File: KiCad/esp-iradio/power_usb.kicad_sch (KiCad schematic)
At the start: 58 parts, among them J201 USB-C TYPE-C-31-M-12, J202 Li-Po cell (JST-PH), Q201 MMBT3904, Q202 MMBT3904, Q203 DMG2305UX-7, SW201 RESET, SW202 BOOT, SW203 ON/OFF MSK12C02, U201 BQ24074RGTR, U202 USBLC6-2SC6, U203 CH340C, U204 DW01A, U205 FS8205A, U206 AP7361C-33Y5-13, U207 TPLP5907MFX-3.3

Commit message: KiCad Rev B: review changes agreed with Grok
Co-Authored-By: Claude Opus 5.5 <noreply@anthropic.com>
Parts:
- added C214: 100nF, Capacitor_SMD:C_0603_1608Metric, symbol Elektuur:C
- added TP203: ESP_EN, TestPoint:TestPoint_Pad_D1.5mm, symbol Connector:TestPoint
- added TP204: ESP_IO0, TestPoint:TestPoint_Pad_D1.5mm, symbol Connector:TestPoint
- added TP205: TXD0, TestPoint:TestPoint_Pad_D1.5mm, symbol Connector:TestPoint
- added TP206: RXD0, TestPoint:TestPoint_Pad_D1.5mm, symbol Connector:TestPoint
- added TP207: GND, TestPoint:TestPoint_Pad_D1.5mm, symbol Connector:TestPoint
- F201: value 1.5A hold -> 2A hold 16V; LCSC C22379952 -> C22374899
- R203: value 33k -> 330k
- R204: value 22k -> 220k
- R210: value 1.1k -> 1.13k
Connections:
- net ESP_EN: now also TP203.1
- net ESP_IO0: now also TP204.1
- net GND: now also C214.2 (-), TP207.1
- net RXD0: now also TP206.1
- net TXD0: now also TP205.1
- net VBUS: no longer D201.1 (K-)
- net VBUS_SENSE: now also C214.1 (+)
- net at C201.1 (+), F201.2 (-), R203.1 (+)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: now also D201.1 (K-)
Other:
- note added: "CHARGER: BQ24074 power path (OUT = VSYS), 0.8 A charge, 1.37 A input"
- note added: "ILIM 1.13k: input 1.37 A, ISET 1.1k: charge 0.8 A"
- note added: "RECOVERY PADS: flash the ESP32 without USB-C / CH340C (switch on, +3V3 = TP4)"
- note removed: "CHARGER: BQ24074 power path (OUT = VSYS), 0.8 A charge, 1.4 A input"
- note removed: "ILIM 1.1k: input 1.4 A, ISET 1.1k: charge 0.8 A"

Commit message: KiCad Rev B: USBLC6 VBUS behind the fuse (third review round)
Co-Authored-By: Claude Opus 5.5 <noreply@anthropic.com>
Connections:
- net VBUS: no longer U202.5 (VBUS)
- net VIN: now reaches C201.1 (+), D201.1 (K-), F201.2 (-), R203.1 (+), TP201.1, U201.13 (IN)
- net VIN: now also U202.5 (VBUS)
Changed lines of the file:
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@@
 		)
 	)
-	(label "VBUS"
+	(label "VIN"
 		(at 60.96 91.44 90)
 		(effects
@@
 		)
 	)
+	(label "VIN"
+		(at 116.84 40.64 0)
+		(effects
+			(font
+				(size 1.27 1.27)
+			)
+			(justify left bottom)
+		)
+	)
 	(no_connect
 		(at 162.56 53.34)
@@
 	(wire
 		(pts
-			(xy 101.6 40.64) (xy 152.4 40.64)
-		)
-		(stroke
+			(xy 101.6 40.64) (xy 116.84 40.64)
+		)
+		(stroke
+			(width 0)
+			(type default)
+		)
+	)
+	(wire
+		(pts
+			(xy 116.84 40.64) (xy 152.4 40.64)
+		)
+		(stroke

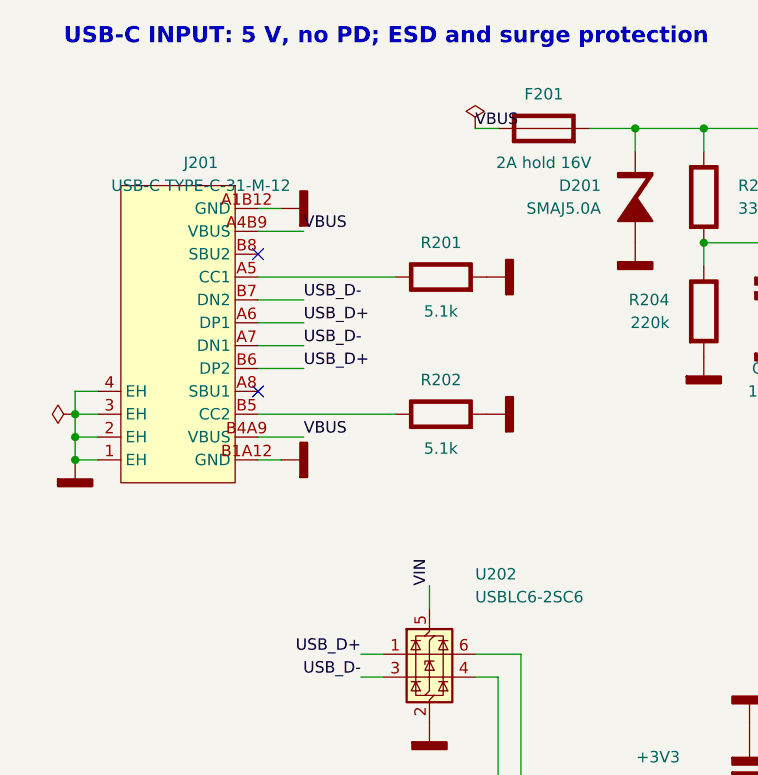
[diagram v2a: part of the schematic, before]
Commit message: KiCad Rev B: first layout (80 x 60 mm, 4 layers, autorouted)
Co-Authored-By: Claude Opus 5.5 <noreply@anthropic.com>
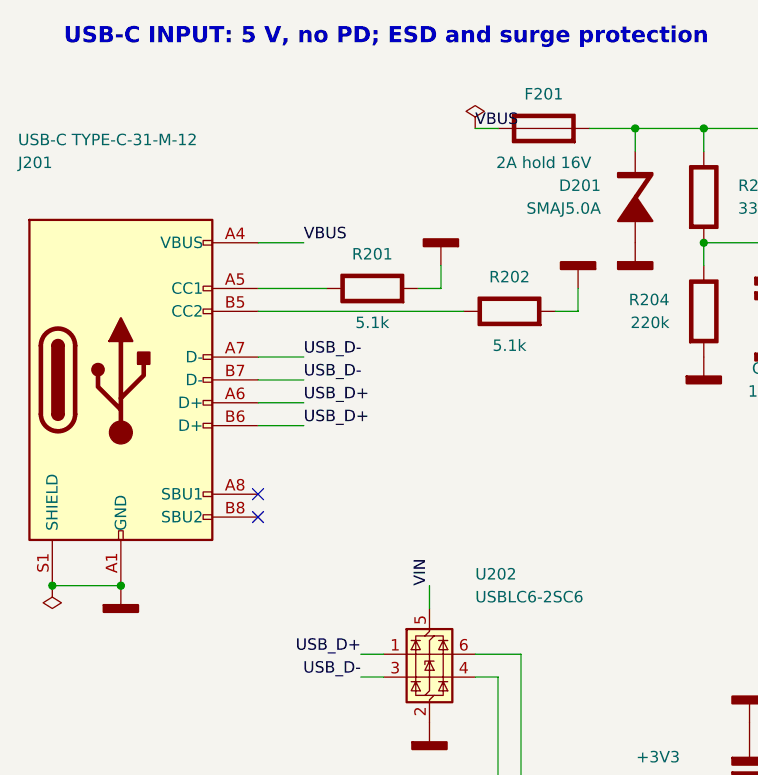
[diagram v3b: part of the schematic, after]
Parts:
- removed J201: USB-C TYPE-C-31-M-12, lcsc:USB-C_SMD-TYPE-C-31-M-12_1, symbol lcsc:TYPE-C-31-M-12
- added J201: USB-C TYPE-C-31-M-12, Connector_USB:USB_C_Receptacle_HRO_TYPE-C-31-M-12, symbol Connector:USB_C_Receptacle_USB2.0_16P
- TP201, TP202, TP203, TP204, TP205, TP206, TP207: now left out of the parts list
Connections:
- net GND: now also J201.A1 (GND), J201.A12 (GND), J201.B1 (GND), J201.B12 (GND), J201.S1 (SHIELD)
- net USB_D+: now also J201.A6 (D+), J201.B6 (D+)
- net USB_D-: now also J201.A7 (D-), J201.B7 (D-)
- net VBUS: now also J201.A4 (VBUS), J201.A9 (VBUS), J201.B4 (VBUS), J201.B9 (VBUS)
- net at R202.1 (+): now also J201.B5 (CC2)
- net at R201.1 (+): now also J201.A5 (CC1)

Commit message: BQ24074RGTT (C2861252) for U201, one BOM line per LCSC part
Co-Authored-By: Claude Opus 5.5 <noreply@anthropic.com>
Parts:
- U201: value BQ24074RGTR -> BQ24074RGTT; LCSC C54313 -> C2861252
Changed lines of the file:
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@@
 			)
 		)
-		(property "Value" "BQ24074RGTR"
+		(property "Value" "BQ24074RGTT"
 			(at 172.72 46.99 0)
 			(effects
@@
 			)
 		)
-		(property "LCSC" "C54313"
+		(property "LCSC" "C2861252"
 			(at 175.26 63.5 0)
 			(effects

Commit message: KiCad Rev C: hand assembly (1206), RCA outputs, display/encoder/connectors floor plan
Co-Authored-By: Claude Opus 5.5 <noreply@anthropic.com>
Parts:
- C201, C202, C203, C208, C209, C210: footprint Capacitor_SMD:C_0805_2012Metric -> Capacitor_SMD:C_1206_3216Metric
- C204, C205, C206, C207, C211, C212, C213, C214: footprint Capacitor_SMD:C_0603_1608Metric -> Capacitor_SMD:C_1206_3216Metric
- D202: footprint LED_SMD:LED_0603_1608Metric -> LED_SMD:LED_1206_3216Metric; LCSC C2286 -> C965822
- D203: footprint LED_SMD:LED_0603_1608Metric -> LED_SMD:LED_1206_3216Metric; LCSC C12624 -> C965825
- D204, D205: value BAT54WS -> BAT54W; footprint Diode_SMD:D_SOD-323 -> Diode_SMD:D_SOD-123; LCSC C7502694 -> C7502705
- R201, R202, R203, R204, R205, R206, R207, R208, R209, R210, R211, R212, R213, R214, R215, R216, R217, R218, R219, R220, R221: footprint Resistor_SMD:R_0603_1608Metric -> Resistor_SMD:R_1206_3216Metric
- RT201: footprint Resistor_SMD:R_0603_1608Metric -> Resistor_SMD:R_0805_2012Metric; LCSC C13564 -> C2889056
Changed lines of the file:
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@@
 			)
 		)
-		(property "Footprint" "Resistor_SMD:R_0603_1608Metric"
+		(property "Footprint" "Resistor_SMD:R_1206_3216Metric"
 			(at 54.61 58.42 0)
 			(effects
@@
 			)
 		)
-		(property "Footprint" "Resistor_SMD:R_0603_1608Metric"
+		(property "Footprint" "Resistor_SMD:R_1206_3216Metric"
 			(at 69.85 60.96 0)
 			(effects
@@
 			)
 		)
-		(property "Footprint" "Resistor_SMD:R_0603_1608Metric"
+		(property "Footprint" "Resistor_SMD:R_1206_3216Metric"
 			(at 91.44 48.26 0)
 			(effects
@@
 			)
 		)
-		(property "Footprint" "Resistor_SMD:R_0603_1608Metric"
+		(property "Footprint" "Resistor_SMD:R_1206_3216Metric"
 			(at 91.44 60.96 0)
 			(effects
@@
 			)
 		)
-		(property "Footprint" "Capacitor_SMD:C_0603_1608Metric"
+		(property "Footprint" "Capacitor_SMD:C_1206_3216Metric"
 			(at 99.06 58.42 0)
 			(effects
@@
 			)
 		)
-		(property "Footprint" "Capacitor_SMD:C_0603_1608Metric"
+		(property "Footprint" "Capacitor_SMD:C_1206_3216Metric"
 			(at 96.52 111.76 0)
 			(effects
@@
 			)
 		)
-		(property "Footprint" "Resistor_SMD:R_0603_1608Metric"
+		(property "Footprint" "Resistor_SMD:R_1206_3216Metric"
 			(at 114.3 137.16 0)
 			(effects
@@
 			)
 		)
-		(property "Footprint" "Resistor_SMD:R_0603_1608Metric"
+		(property "Footprint" "Resistor_SMD:R_1206_3216Metric"
 			(at 114.3 162.56 0)
 			(effects
@@
 			)
 		)
-		(property "Footprint" "Resistor_SMD:R_0603_1608Metric"
+		(property "Footprint" "Resistor_SMD:R_1206_3216Metric"
 			(at 139.7 121.92 0)
 			(effects
@@
 			)
 		)
-		(property "Footprint" "Capacitor_SMD:C_0603_1608Metric"
+		(property "Footprint" "Capacitor_SMD:C_1206_3216Metric"
 			(at 147.32 132.08 0)
 			(effects
@@
 			)
 		)
-		(property "Footprint" "Resistor_SMD:R_0603_1608Metric"
+		(property "Footprint" "Resistor_SMD:R_1206_3216Metric"
 			(at 139.7 147.32 0)
 			(effects
@@
 			)
 		)
-		(property "Footprint" "Capacitor_SMD:C_0805_2012Metric"
+		(property "Footprint" "Capacitor_SMD:C_1206_3216Metric"
 			(at 152.4 45.72 0)
 			(effects
@@
 			)
 		)
-		(property "Footprint" "Resistor_SMD:R_0603_1608Metric"
+		(property "Footprint" "Resistor_SMD:R_1206_3216Metric"
 			(at 116.84 93.98 0)
 			(effects
@@
 			)
 		)
-		(property "Footprint" "Resistor_SMD:R_0603_1608Metric"
+		(property "Footprint" "Resistor_SMD:R_1206_3216Metric"
 			(at 147.32 93.98 0)
 			(effects
@@
 			)
 		)
-		(property "Footprint" "Resistor_SMD:R_0603_1608Metric"
+		(property "Footprint" "Resistor_SMD:R_1206_3216Metric"
 			(at 160.02 93.98 0)
 			(effects
@@
 			)
 		)
-		(property "Footprint" "Capacitor_SMD:C_0805_2012Metric"
+		(property "Footprint" "Capacitor_SMD:C_1206_3216Metric"
 			(at 198.12 40.64 0)
 			(effects
@@
 			)
 		)
-		(property "Footprint" "Resistor_SMD:R_0603_1608Metric"
+		(property "Footprint" "Resistor_SMD:R_0805_2012Metric"
 			(at 213.36 71.12 0)
 			(effects
@@
 			)
 		)
-		(property "LCSC" "C13564"
+		(property "LCSC" "C2889056"
 			(at 213.36 71.12 0)
 			(effects
@@
 			)
 		)
-		(property "Footprint" "Resistor_SMD:R_0603_1608Metric"
+		(property "Footprint" "Resistor_SMD:R_1206_3216Metric"
 			(at 175.26 101.6 0)
 			(effects
@@
 			)
 		)
-		(property "Footprint" "LED_SMD:LED_0603_1608Metric"
+		(property "Footprint" "LED_SMD:LED_1206_3216Metric"
 			(at 185.42 101.6 0)
 			(effects
@@
 			)
 		)
-		(property "LCSC" "C2286"
+		(property "LCSC" "C965822"
 			(at 185.42 101.6 0)
 			(effects
@@
 			)
 		)
-		(property "Value" "BAT54WS"
+		(property "Value" "BAT54W"
 			(at 203.2 105.41 90)
 			(effects
@@
 			)
 		)
-		(property "Footprint" "Diode_SMD:D_SOD-323"
+		(property "Footprint" "Diode_SMD:D_SOD-123"
 			(at 203.2 101.6 0)
 			(effects
@@
 			)
 		)
-		(property "LCSC" "C7502694"
+		(property "LCSC" "C7502705"
 			(at 203.2 101.6 0)
 			(effects
@@
 			)
 		)
-		(property "Footprint" "Resistor_SMD:R_0603_1608Metric"
+		(property "Footprint" "Resistor_SMD:R_1206_3216Metric"
 			(at 213.36 96.52 0)
 			(effects
@@
 			)
 		)
-		(property "Footprint" "Resistor_SMD:R_0603_1608Metric"
+		(property "Footprint" "Resistor_SMD:R_1206_3216Metric"
 			(at 175.26 116.84 0)
 			(effects
@@
 			)
 		)
-		(property "Footprint" "LED_SMD:LED_0603_1608Metric"
+		(property "Footprint" "LED_SMD:LED_1206_3216Metric"
 			(at 185.42 116.84 0)
 			(effects
@@
 			)
 		)
-		(property "LCSC" "C12624"
+		(property "LCSC" "C965825"
 			(at 185.42 116.84 0)
 			(effects
@@
 			)
 		)
-		(property "Value" "BAT54WS"
+		(property "Value" "BAT54W"
 			(at 203.2 120.65 90)
 			(effects
@@
 			)
 		)
-		(property "Footprint" "Diode_SMD:D_SOD-323"
+		(property "Footprint" "Diode_SMD:D_SOD-123"
 			(at 203.2 116.84 0)
 			(effects
@@
 			)
 		)
-		(property "LCSC" "C7502694"
+		(property "LCSC" "C7502705"
 			(at 203.2 116.84 0)
 			(effects
@@
 			)
 		)
-		(property "Footprint" "Resistor_SMD:R_0603_1608Metric"
+		(property "Footprint" "Resistor_SMD:R_1206_3216Metric"
 			(at 213.36 111.76 0)
 			(effects
@@
 			)
 		)
-		(property "Footprint" "Resistor_SMD:R_0603_1608Metric"
+		(property "Footprint" "Resistor_SMD:R_1206_3216Metric"
 			(at 246.38 76.2 0)
 			(effects
@@
 			)
 		)
-		(property "Footprint" "Capacitor_SMD:C_0805_2012Metric"
+		(property "Footprint" "Capacitor_SMD:C_1206_3216Metric"
 			(at 223.52 66.04 0)
 			(effects
@@
 			)
 		)
-		(property "Footprint" "Resistor_SMD:R_0603_1608Metric"
+		(property "Footprint" "Resistor_SMD:R_1206_3216Metric"
 			(at 340.36 60.96 0)
 			(effects
@@
 			)
 		)
-		(property "Footprint" "Resistor_SMD:R_0603_1608Metric"
+		(property "Footprint" "Resistor_SMD:R_1206_3216Metric"
 			(at 340.36 73.66 0)
 			(effects
@@
 			)
 		)
-		(property "Footprint" "Capacitor_SMD:C_0603_1608Metric"
+		(property "Footprint" "Capacitor_SMD:C_1206_3216Metric"
 			(at 347.98 73.66 0)
 			(effects
@@
 			)
 		)
-		(property "Footprint" "Resistor_SMD:R_0603_1608Metric"
+		(property "Footprint" "Resistor_SMD:R_1206_3216Metric"
 			(at 261.62 76.2 0)
 			(effects
@@
 			)
 		)
-		(property "Footprint" "Capacitor_SMD:C_0603_1608Metric"
+		(property "Footprint" "Capacitor_SMD:C_1206_3216Metric"
 			(at 254 96.52 0)
 			(effects
@@
 			)
 		)
-		(property "Footprint" "Resistor_SMD:R_0603_1608Metric"
+		(property "Footprint" "Resistor_SMD:R_1206_3216Metric"
 			(at 292.1 96.52 0)
 			(effects
@@
 			)
 		)
-		(property "Footprint" "Capacitor_SMD:C_0805_2012Metric"
+		(property "Footprint" "Capacitor_SMD:C_1206_3216Metric"
 			(at 279.4 187.96 0)
 			(effects
@@
 			)
 		)
-		(property "Footprint" "Capacitor_SMD:C_0805_2012Metric"
+		(property "Footprint" "Capacitor_SMD:C_1206_3216Metric"
 			(at 281.94 172.72 0)
 			(effects
@@
 			)
 		)
-		(property "Footprint" "Capacitor_SMD:C_0805_2012Metric"
+		(property "Footprint" "Capacitor_SMD:C_1206_3216Metric"
 			(at 292.1 172.72 0)
 			(effects
@@
 			)
 		)
-		(property "Footprint" "Capacitor_SMD:C_0603_1608Metric"
+		(property "Footprint" "Capacitor_SMD:C_1206_3216Metric"
 			(at 302.26 172.72 0)
 			(effects
@@
 			)
 		)
-		(property "Footprint" "Resistor_SMD:R_0603_1608Metric"
+		(property "Footprint" "Resistor_SMD:R_1206_3216Metric"
 			(at 236.22 167.64 0)
 			(effects
@@
 			)
 		)
-		(property "Footprint" "Capacitor_SMD:C_0603_1608Metric"
+		(property "Footprint" "Capacitor_SMD:C_1206_3216Metric"
 			(at 236.22 223.52 0)
 			(effects
@@
 			)
 		)
-		(property "Footprint" "Capacitor_SMD:C_0603_1608Metric"
+		(property "Footprint" "Capacitor_SMD:C_1206_3216Metric"
 			(at 264.16 223.52 0)
 			(effects

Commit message: 3D models for the USB-C and the encoder (project footprints, EasyEDA models)
Co-Authored-By: Claude Opus 5.5 <noreply@anthropic.com>
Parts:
- J201: footprint Connector_USB:USB_C_Receptacle_HRO_TYPE-C-31-M-12 -> esp-iradio:USB_C_Receptacle_HRO_TYPE-C-31-M-12
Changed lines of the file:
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@@
 			)
 		)
-		(property "Footprint" "Connector_USB:USB_C_Receptacle_HRO_TYPE-C-31-M-12"
+		(property "Footprint" "esp-iradio:USB_C_Receptacle_HRO_TYPE-C-31-M-12"
 			(at 26.67 68.58 0)
 			(effects
